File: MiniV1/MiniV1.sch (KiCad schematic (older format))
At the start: 18 parts

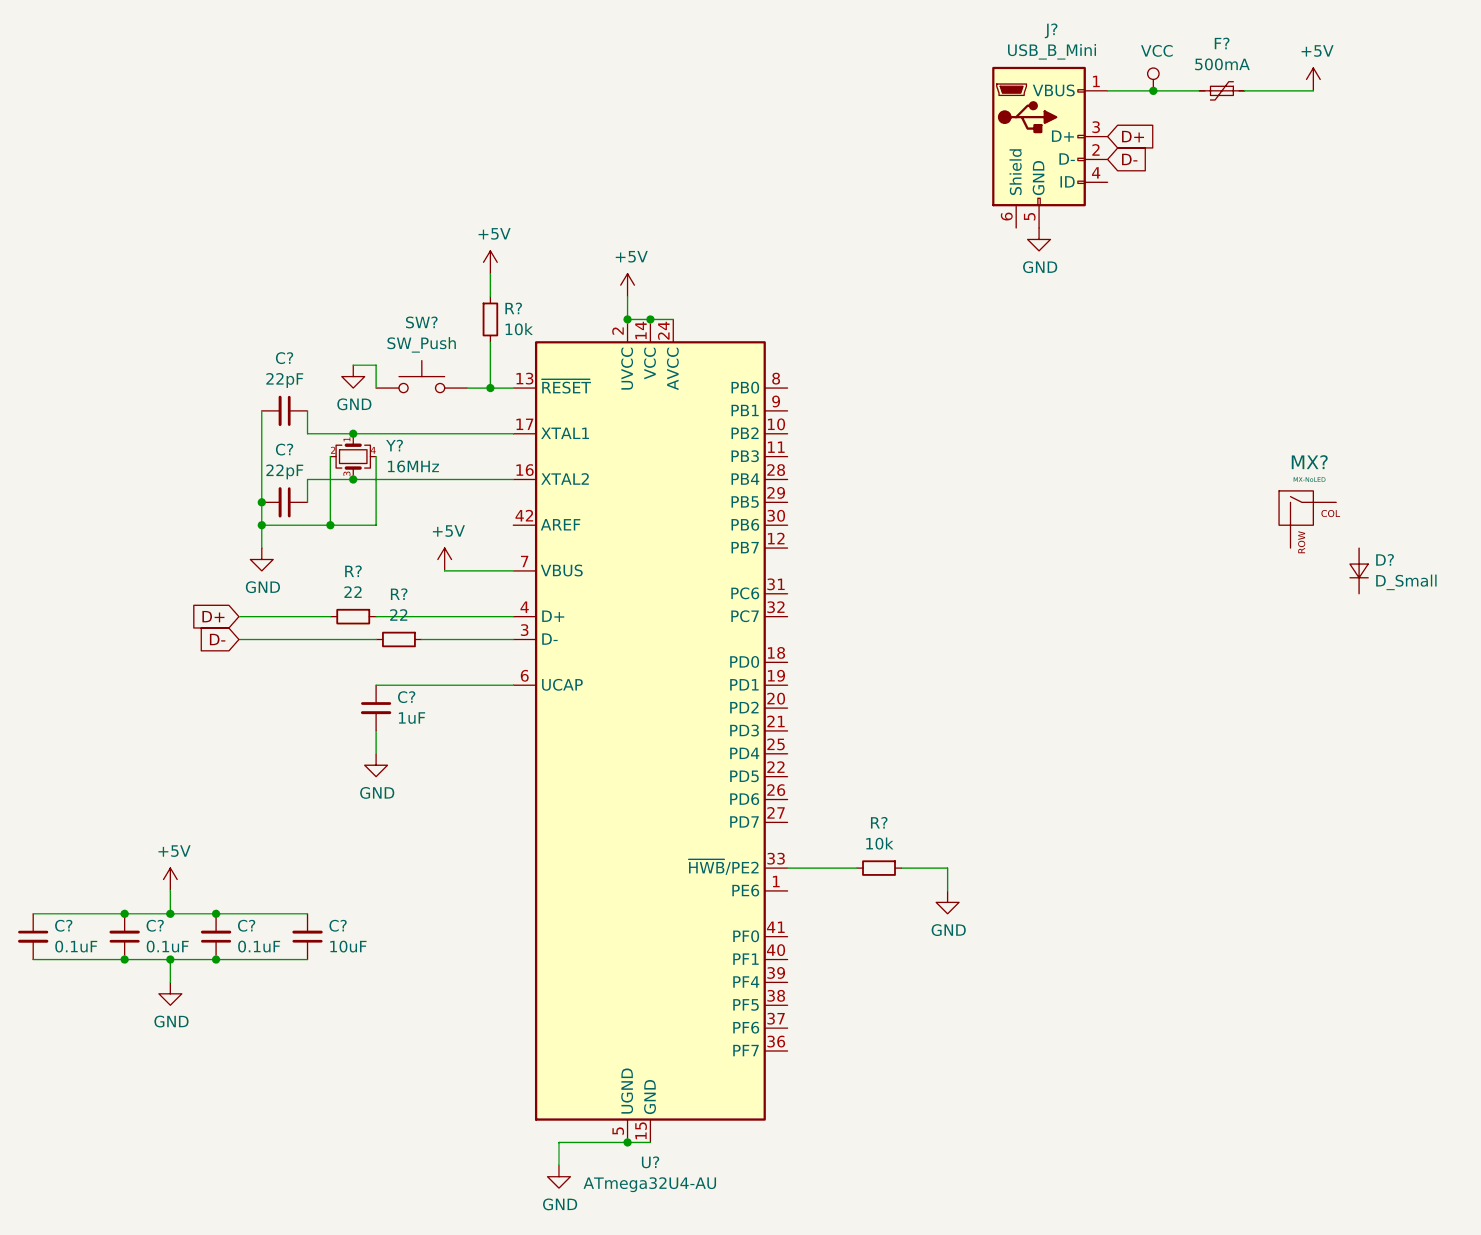
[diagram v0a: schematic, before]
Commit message: Updated the footprint setup
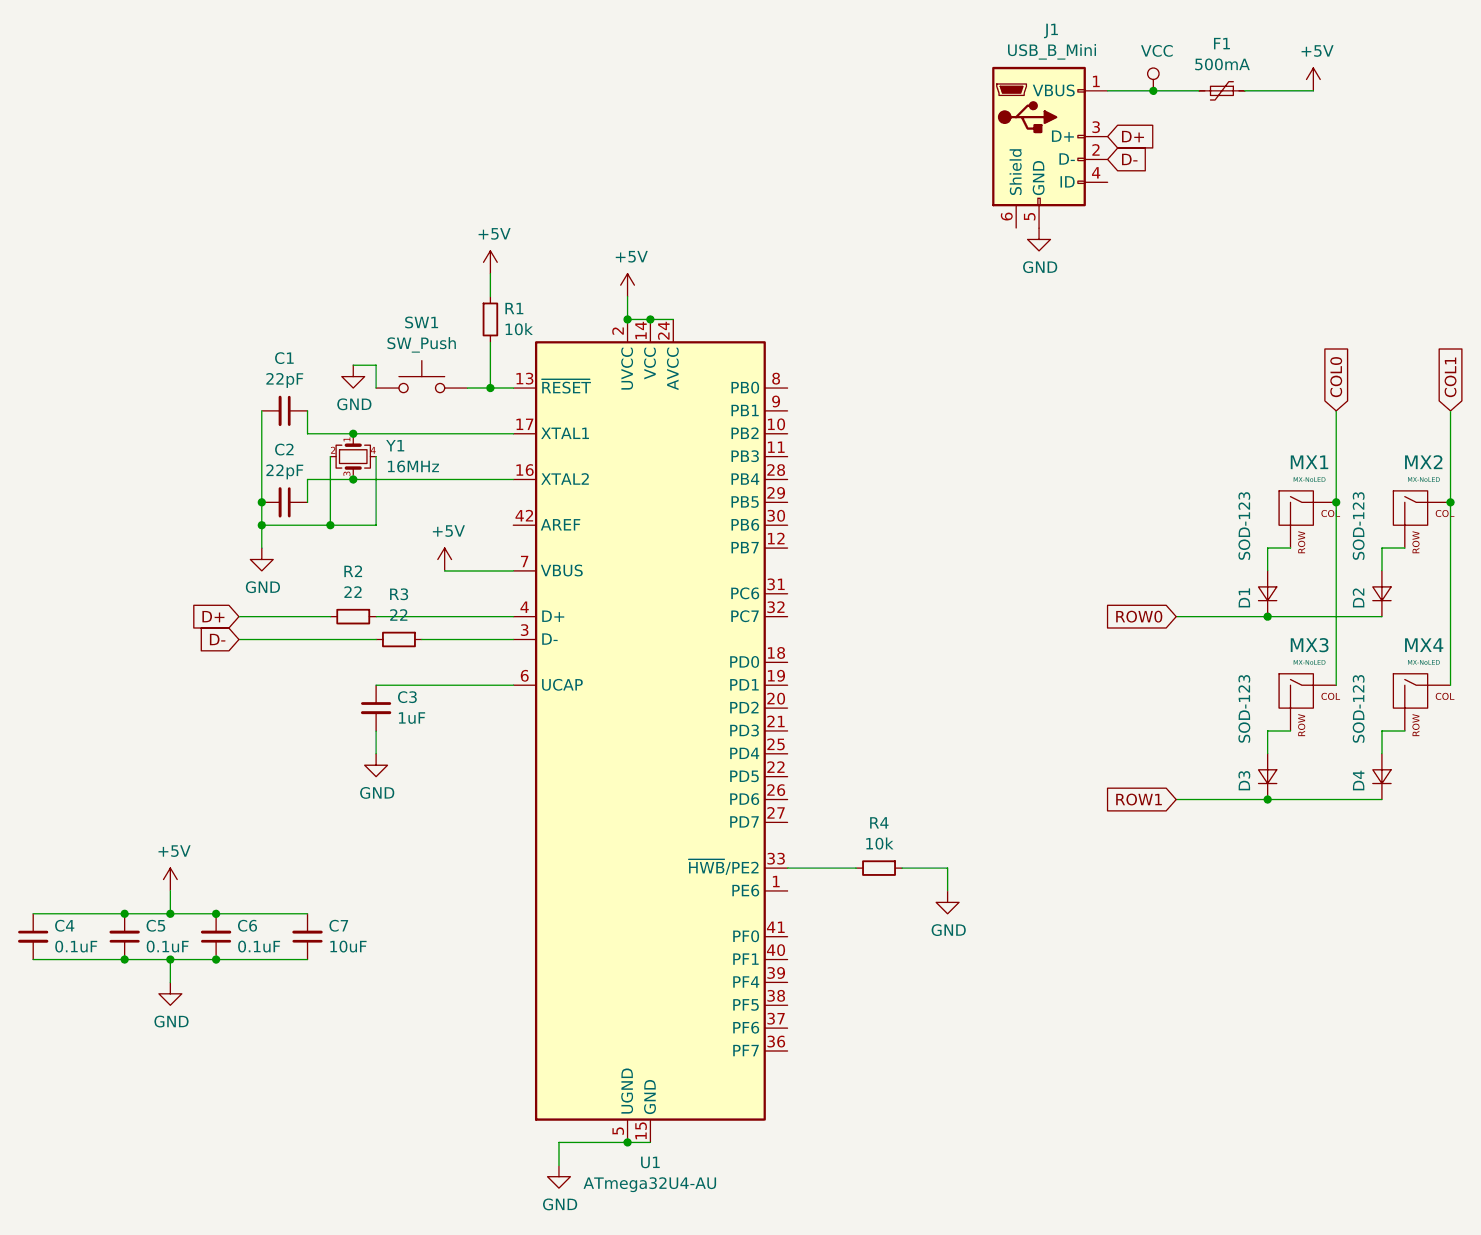
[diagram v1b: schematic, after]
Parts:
- added D2, D3, D4: SOD-123, Diode_SMD:D_SOD-123, symbol Device:D_Small
- added MX2, MX3, MX4: MX-NoLED, acheron_MX:MX100, symbol MX_Alps_Hybrid:MX-NoLED
- C1, C2, C3, C4, C5, C6, C7: renamed from C?; footprint (none) -> Capacitor_SMD:C_0805_2012Metric
- D1: renamed from D?; value D_Small -> SOD-123; footprint (none) -> Diode_SMD:D_SOD-123
- F1: renamed from F?; footprint (none) -> Fuse:Fuse_1206_3216Metric
- J1: renamed from J?; footprint (none) -> acheron_Connectors:USB_MiniB_XM7D-0512
- MX1: renamed from MX?; footprint (none) -> acheron_MX:MX100
- gave numbers to parts that had none: 7
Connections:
- net COL0: now reaches MX1.1 (COL)
- net COL0: now also MX3.1 (COL)
- net at MX1.2 (ROW): now also D1.2 (A)
- net ROW0: now reaches D1.1 (K)
- net ROW0: now also D2.1 (K)
- new net: D2.2 (A), MX2.2 (ROW)
- new net: D3.2 (A), MX3.2 (ROW)
- new net: D4.2 (A), MX4.2 (ROW)
- new net COL1: MX2.1 (COL), MX4.1 (COL)
- new net ROW1: D3.1 (K), D4.1 (K)
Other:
- moved on the sheet: D1

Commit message: Schematic Finished
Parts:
- MX1, MX2, MX3, MX4: footprint acheron_MX:MX100 -> MX_Only:MXOnly-1U-NoLED
- R1, R2, R3, R4: footprint (none) -> Resistor_SMD:R_0805_2012Metric
- SW1: footprint (none) -> random-keyboard-parts:SKQG-1155865
- Y1: footprint (none) -> Crystal:Crystal_SMD_3225-4Pin_3.2x2.5mm
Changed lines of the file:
@@
 F 0 "R4" V 4304 5900 50  0000 C CNN
 F 1 "10k" V 4395 5900 50  0000 C CNN
-F 2 "" H 4500 5900 50  0001 C CNN
+F 2 "Resistor_SMD:R_0805_2012Metric" H 4500 5900 50  0001 C CNN
 F 3 "~" H 4500 5900 50  0001 C CNN
 	1    4500 5900
@@
 F 0 "R2" V 2004 4800 50  0000 C CNN
 F 1 "22" V 2095 4800 50  0000 C CNN
-F 2 "" H 2200 4800 50  0001 C CNN
+F 2 "Resistor_SMD:R_0805_2012Metric" H 2200 4800 50  0001 C CNN
 F 3 "~" H 2200 4800 50  0001 C CNN
 	1    2200 4800
@@
 F 0 "R3" V 2204 4900 50  0000 C CNN
 F 1 "22" V 2295 4900 50  0000 C CNN
-F 2 "" H 2400 4900 50  0001 C CNN
+F 2 "Resistor_SMD:R_0805_2012Metric" H 2400 4900 50  0001 C CNN
 F 3 "~" H 2400 4900 50  0001 C CNN
 	1    2400 4900
@@
 F 0 "Y1" V 2154 4244 50  0000 L CNN
 F 1 "16MHz" V 2245 4244 50  0000 L CNN
-F 2 "" H 2200 4100 50  0001 C CNN
+F 2 "Crystal:Crystal_SMD_3225-4Pin_3.2x2.5mm" H 2200 4100 50  0001 C CNN
 F 3 "~" H 2200 4100 50  0001 C CNN
 	1    2200 4100
@@
 F 0 "SW1" H 2500 4085 50  0000 C CNN
 F 1 "SW_Push" H 2500 3994 50  0000 C CNN
-F 2 "" H 2500 4000 50  0001 C CNN
+F 2 "random-keyboard-parts:SKQG-1155865" H 2500 4000 50  0001 C CNN
 F 3 "~" H 2500 4000 50  0001 C CNN
 	1    2500 3800
@@
 F 0 "R1" H 2859 3546 50  0000 L CNN
 F 1 "10k" H 2859 3455 50  0000 L CNN
-F 2 "" H 2800 3500 50  0001 C CNN
+F 2 "Resistor_SMD:R_0805_2012Metric" H 2800 3500 50  0001 C CNN
 F 3 "~" H 2800 3500 50  0001 C CNN
 	1    2800 3500
@@
 F 0 "MX1" H 6383 4573 60  0000 C CNN
 F 1 "MX-NoLED" H 6383 4499 20  0000 C CNN
-F 2 "acheron_MX:MX100" H 5725 4325 60  0001 C CNN
+F 2 "MX_Only:MXOnly-1U-NoLED" H 5725 4325 60  0001 C CNN
 F 3 "" H 5725 4325 60  0001 C CNN
 	1    6350 4350
@@
 F 0 "MX2" H 6883 4573 60  0000 C CNN
 F 1 "MX-NoLED" H 6883 4499 20  0000 C CNN
-F 2 "acheron_MX:MX100" H 6225 4325 60  0001 C CNN
+F 2 "MX_Only:MXOnly-1U-NoLED" H 6225 4325 60  0001 C CNN
 F 3 "" H 6225 4325 60  0001 C CNN
 	1    6850 4350
@@
 F 0 "MX3" H 6383 5373 60  0000 C CNN
 F 1 "MX-NoLED" H 6383 5299 20  0000 C CNN
-F 2 "acheron_MX:MX100" H 5725 5125 60  0001 C CNN
+F 2 "MX_Only:MXOnly-1U-NoLED" H 5725 5125 60  0001 C CNN
 F 3 "" H 5725 5125 60  0001 C CNN
 	1    6350 5150
@@
 F 0 "MX4" H 6883 5373 60  0000 C CNN
 F 1 "MX-NoLED" H 6883 5299 20  0000 C CNN
-F 2 "acheron_MX:MX100" H 6225 5125 60  0001 C CNN
+F 2 "MX_Only:MXOnly-1U-NoLED" H 6225 5125 60  0001 C CNN
 F 3 "" H 6225 5125 60  0001 C CNN
 	1    6850 5150

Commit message: Fingers Crossed test board done
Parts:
- J1: footprint acheron_Connectors:USB_MiniB_XM7D-0512 -> random-keyboard-parts:Molex-0548190589; symbol Connector:USB_B_Mini -> random-keyboard-parts:Molex-0548190589
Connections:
- net COL0: now also U1.29 (PB5)
- net COL1: now also U1.28 (PB4)
- net D-: now also J1.4 (D-); no longer J1.2 (D-)
- net GND: now also J1.1 (GND); no longer J1.5 (GND)
- net ROW0: now also U1.27 (PD7)
- net ROW1: now also U1.30 (PB6)
- net VCC: now also J1.5 (VBUS); no longer J1.1 (VBUS)
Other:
- moved on the sheet: F1
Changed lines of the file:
@@
 	1    0    0    -1
 $EndComp
-Text GLabel 5500 2800 2    50   Input ~ 0
+Text GLabel 5080 2650 2    50   Input ~ 0
 D-
-Text GLabel 5500 2700 2    50   Input ~ 0
+Text GLabel 5080 2750 2    50   Input ~ 0
 D+
 $Comp
 L power:VCC #PWR01
 U 1 1 5DFE7759
-P 5700 2500
-F 0 "#PWR01" H 5700 2350 50  0001 C CNN
-F 1 "VCC" H 5717 2673 50  0000 C CNN
-F 2 "" H 5700 2500 50  0001 C CNN
-F 3 "" H 5700 2500 50  0001 C CNN
-	1    5700 2500
+P 5280 2550
+F 0 "#PWR01" H 5280 2400 50  0001 C CNN
+F 1 "VCC" H 5297 2723 50  0000 C CNN
+F 2 "" H 5280 2550 50  0001 C CNN
+F 3 "" H 5280 2550 50  0001 C CNN
+	1    5280 2550
 	1    0    0    -1
 $EndComp
@@
 L power:+5V #PWR02
 U 1 1 5DFE50FE
-P 6400 2500
-F 0 "#PWR02" H 6400 2350 50  0001 C CNN
-F 1 "+5V" H 6415 2673 50  0000 C CNN
-F 2 "" H 6400 2500 50  0001 C CNN
-F 3 "" H 6400 2500 50  0001 C CNN
-	1    6400 2500
+P 5980 2550
+F 0 "#PWR02" H 5980 2400 50  0001 C CNN
+F 1 "+5V" H 5995 2723 50  0000 C CNN
+F 2 "" H 5980 2550 50  0001 C CNN
+F 3 "" H 5980 2550 50  0001 C CNN
+	1    5980 2550
 	1    0    0    -1
 $EndComp
@@
 L Device:Polyfuse_Small F1
 U 1 1 5DFE3369
-P 6000 2500
-F 0 "F1" V 5795 2500 50  0000 C CNN
-F 1 "500mA" V 5886 2500 50  0000 C CNN
-F 2 "Fuse:Fuse_1206_3216Metric" H 6050 2300 50  0001 L CNN
-F 3 "~" H 6000 2500 50  0001 C CNN
-	1    6000 2500
+P 5580 2550
+F 0 "F1" V 5375 2550 50  0000 C CNN
+F 1 "500mA" V 5466 2550 50  0000 C CNN
+F 2 "Fuse:Fuse_1206_3216Metric" H 5630 2350 50  0001 L CNN
+F 3 "~" H 5580 2550 50  0001 C CNN
+	1    5580 2550
 	0    1    1    0
 $EndComp
 $Comp
-L Connector:USB_B_Mini J1
+L random-keyboard-parts:Molex-0548190589 J1
 U 1 1 5DFDD546
-P 5200 2700
-F 0 "J1" H 5257 3167 50  0000 C CNN
-F 1 "USB_B_Mini" H 5257 3076 50  0000 C CNN
-F 2 "acheron_Connectors:USB_MiniB_XM7D-0512" H 5350 2650 50  0001 C CNN
-F 3 "~" H 5350 2650 50  0001 C CNN
-	1    5200 2700
-	1    0    0    -1
-$EndComp
-Wire Wire Line
-	5500 2500 5700 2500
-Connection ~ 5700 2500
-Wire Wire Line
-	5700 2500 5900 2500
-Wire Wire Line
-	6100 2500 6400 2500
+P 4780 2750
+F 0 "J1" H 4837 3217 50  0000 C CNN
+F 1 "USB_B_Mini" H 4837 3126 50  0000 C CNN
+F 2 "random-keyboard-parts:Molex-0548190589" H 4930 2700 50  0001 C CNN
+F 3 "~" H 4930 2700 50  0001 C CNN
+	1    4780 2750
+	0    -1   -1   0
+$EndComp
+Wire Wire Line
+	5080 2550 5280 2550
+Connection ~ 5280 2550
+Wire Wire Line
+	5280 2550 5480 2550
+Wire Wire Line
+	5680 2550 5980 2550
 $Comp
 L MX_Alps_Hybrid:MX-NoLED MX1
@@
 Text GLabel 7000 3900 1    50   Input ~ 0
 COL1
+Wire Wire Line
+	5080 2950 5200 2950
+Wire Wire Line
+	5200 2950 5200 3100
+Text GLabel 4100 5700 2    50   Input ~ 0
+ROW0
+Text GLabel 4100 4400 2    50   Input ~ 0
+ROW1
+Text GLabel 4100 4300 2    50   Input ~ 0
+COL0
+Text GLabel 4100 4200 2    50   Input ~ 0
+COL1
 $EndSCHEMATC
